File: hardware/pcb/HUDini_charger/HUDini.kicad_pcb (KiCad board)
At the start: 2 copper layers, 100 x 24 mm, 46 parts, among them J1 USB_C_Receptacle_PowerOnly_6P, J2 Conn_01x06_Pin, J3 Conn_01x06_Pin, J4 Conn_01x07_Pin, Q1 CHG (GDS), Q2 DSG (GDS), SW1 RESET, SW3 PWR_REC, U2 LM3671, U3 BQ29700DSER, U4 MCP73831-2-OT, U5 MDBT42Q-512K

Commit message: Updated PCB Files
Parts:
- removed C10: 100uF, Capacitor_SMD:C_0603_1608Metric
- removed C2: 10uF, Capacitor_SMD:C_0603_1608Metric
- removed C3: 0.1uF, Capacitor_SMD:C_0603_1608Metric
- removed D2, D3: D_Zener_Filled, Diode_SMD:D_SOD-323
- removed J1: USB_C_Receptacle_PowerOnly_6P, Connector_USB:USB_C_Receptacle_HRO_TYPE-C-31-M-12
- removed L1: 2.2uH, Inductor_SMD:L_1210_3225Metric
- removed U5: MDBT42Q-512K, RF_Module:Raytac_MDBT42Q
- added BT2: LIR2450, Connector_Wire:SolderWire-0.15sqmm_1x02_P4mm_D0.5mm_OD1.5mm, F.Cu at (167.5, 123.0)
- added C12: 10uF, Capacitor_SMD:C_0603_1608Metric_Pad1.08x0.95mm_HandSolder, F.Cu at (175.2, 72.0)
- added C13: 0.1uF, Capacitor_SMD:C_0603_1608Metric_Pad1.08x0.95mm_HandSolder, F.Cu at (175.2, 74.5)
- added C14: 10uF, Capacitor_SMD:C_0603_1608Metric_Pad1.08x0.95mm_HandSolder, F.Cu at (175.2, 77.0)
- added C15: 10uF, Capacitor_SMD:C_0603_1608Metric_Pad1.08x0.95mm_HandSolder, F.Cu at (175.2, 79.5)
- added J5: USB_C_Receptacle_USB2.0_14P, Connector_USB:USB_C_Receptacle_GCT_USB4085, F.Cu at (176.7, 122.6)
- added L2: 1.5uH, Inductor_SMD:L_0603_1608Metric_Pad1.05x0.95mm_HandSolder, F.Cu at (175.2, 82.1)
- added R18: 10K, Resistor_SMD:R_0603_1608Metric_Pad0.98x0.95mm_HandSolder, F.Cu at (246.6, 116.5)
- added R19: 10K, Resistor_SMD:R_0603_1608Metric_Pad0.98x0.95mm_HandSolder, F.Cu at (254.9, 122.5)
- added R20: 330, Resistor_SMD:R_0603_1608Metric_Pad0.98x0.95mm_HandSolder, F.Cu at (246.6, 122.5)
- added REF**: MountingHole_2.2mm_M2_DIN965_Pad, MountingHole:MountingHole_2.2mm_M2_DIN965_Pad, F.Cu at (167.5, 129.5)
- added REF**: MountingHole_2.2mm_M2_DIN965_Pad, MountingHole:MountingHole_2.2mm_M2_DIN965_Pad, F.Cu at (167.5, 112.5)
- added REF**: MountingHole_2.2mm_M2_DIN965_Pad, MountingHole:MountingHole_2.2mm_M2_DIN965_Pad, F.Cu at (262.5, 112.5)
- added REF**: MountingHole_2.2mm_M2_DIN965_Pad, MountingHole:MountingHole_2.2mm_M2_DIN965_Pad, F.Cu at (262.5, 129.5)
- added SW2: BOOT, Button_Switch_SMD:SW_SPST_PTS810, F.Cu at (241.5, 117.0)
- added SW5: SW_SPDT, Button_Switch_THT:SW_E-Switch_EG1224_SPDT_Angled, F.Cu at (189.5, 125.5)
- added U1: TPS63031DSK, Package_SON:WSON-10-1EP_2.5x2.5mm_P0.5mm_EP1.2x2mm, F.Cu at (180.2, 92.8)
- BT1: footprint Battery:BatteryHolder_Keystone_3009_1x2450 -> Connector_Wire:SolderWire-0.15sqmm_1x02_P4mm_D0.5mm_OD1.5mm
- C1: value 22uF -> 0.1uF; footprint Capacitor_SMD:C_0603_1608Metric -> Capacitor_SMD:C_0603_1608Metric_Pad1.08x0.95mm_HandSolder
- C11, C4, C5, C6, C8, C9: footprint Capacitor_SMD:C_0603_1608Metric -> Capacitor_SMD:C_0603_1608Metric_Pad1.08x0.95mm_HandSolder
- C7: value 1uF -> 10uF; footprint Capacitor_SMD:C_0603_1608Metric -> Capacitor_SMD:C_0603_1608Metric_Pad1.08x0.95mm_HandSolder
- D1, D4: footprint LED_SMD:LED_0603_1608Metric -> LED_SMD:LED_0603_1608Metric_Pad1.05x0.95mm_HandSolder
- J2: value Conn_01x06_Pin -> Conn_01x04_Pin; footprint Connector_PinHeader_2.54mm:PinHeader_1x06_P2.54mm_Vertical -> Connector_Wire:SolderWire-0.15sqmm_1x04_P4mm_D0.5mm_OD1.5mm
- J3: footprint Connector_PinHeader_2.54mm:PinHeader_1x06_P2.54mm_Vertical -> Connector_Wire:SolderWire-0.15sqmm_1x06_P4mm_D0.5mm_OD1.5mm
- J4: footprint Connector_PinHeader_2.54mm:PinHeader_1x07_P2.54mm_Horizontal -> Connector_PinHeader_1.00mm:PinHeader_1x07_P1.00mm_Horizontal
- R1, R12, R13, R14, R15, R16, R17, R2, R3, R4, R5, R6, R7, R8: footprint Resistor_SMD:R_0603_1608Metric -> Resistor_SMD:R_0603_1608Metric_Pad0.98x0.95mm_HandSolder
- R10: value 10K -> 22; footprint Resistor_SMD:R_0603_1608Metric -> Resistor_SMD:R_0603_1608Metric_Pad0.98x0.95mm_HandSolder
- R11: value 330 -> 22; footprint Resistor_SMD:R_0603_1608Metric -> Resistor_SMD:R_0603_1608Metric_Pad0.98x0.95mm_HandSolder
- R9: value 100K -> 10K; footprint Resistor_SMD:R_0603_1608Metric -> Resistor_SMD:R_0603_1608Metric_Pad0.98x0.95mm_HandSolder
- U2: value LM3671 -> ESP32-S3-MINI-1; footprint Package_TO_SOT_SMD:SOT-23-5 -> RF_Module:ESP32-S2-MINI-1
- moved SW3 151.3 mm to (254.0, 128.2)
- moved C9 146.8 mm to (258.9, 116.5)
- moved R13 142.8 mm to (258.9, 119.5)
- moved R12 138.6 mm to (254.8, 119.5)
- moved R14 138.5 mm to (259.0, 122.5)
- moved R17 134.8 mm to (254.8, 116.5)
- moved C11 134.6 mm to (246.6, 119.5)
- moved R15 130.3 mm to (250.7, 116.5)
- moved R16 130.3 mm to (250.7, 119.5)
- moved D4 126.2 mm to (250.8, 122.5)
- moved C8 123.8 mm to (235.9, 116.0)
- moved C7 123.4 mm to (235.9, 125.0)
- moved C6 123.4 mm to (235.9, 122.0)
- moved R9 119.4 mm to (235.9, 119.0)
- moved SW1 115.6 mm to (241.5, 122.5)
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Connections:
- BT1 pad 1: VBAT -> +BATT
- C1 pad 1: VBAT -> Net-(U3-BAT)
- C1 pad 2: GND -> B_GND
- C11 pad 1: GND -> Net-(U2-EN)
- C11 pad 2: Net-(U5-DEC4) -> GND
- C4 pad 1: VBAT -> +BATT
- J2 pad 3: /SWDCLK -> /UART_TX
- J2 pad 4: /SWDIO -> /UART_RX
- R10 pad 1: +3V3 -> USB_D-
- R10 pad 2: /BTN_PWRREC -> Net-(U2-USB_D-)
- R11 pad 1: /REC_LED -> USB_D+
- R11 pad 2: Net-(D4-A) -> Net-(U2-USB_D+)
- R13 pad 2: Net-(U5-TRACEDATA1/P0.16) -> Net-(U2-IO12)
- R14 pad 2: Net-(U5-TRACEDATA2/P0.15) -> Net-(U2-IO11)
- R15 pad 2: Net-(U5-P0.11) -> Net-(U2-IO4)
- R16 pad 2: Net-(U5-P0.12) -> Net-(U2-IO5)
- R17 pad 2: Net-(U5-P0.13) -> Net-(U2-IO6)
- R4 pad 1: VBAT -> +BATT
- R9 pad 1: /RESET -> Net-(U2-EN)
- SW1 pad 1: /RESET -> Net-(U2-EN)
- SW3 pad 1: /BTN_PWRREC -> /BTN_REC
- U2 pad 1: VBAT -> GND
- U2 pad 3: VBAT -> +3V3
- U2 pad 4: +3V3 -> Net-(U2-IO0)
- U2 pad 5: Net-(U2-SW) -> unconnected-(U2-IO1-Pad5)
- U4 pad 3: VBAT -> +BATT
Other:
- board size 100 x 24 mm -> 100 x 22 mm
- copper layers 2 -> 4

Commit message: new files
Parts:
- removed L2: 1.5uH, Inductor_SMD:L_0603_1608Metric_Pad1.05x0.95mm_HandSolder
- added L1: LPS3015-153MRC, footprints:IND_LPS3015_COC, F.Cu at (128.8, 92.1)
- C4, C5, C8: footprint Capacitor_SMD:C_0603_1608Metric_Pad1.08x0.95mm_HandSolder -> Capacitor_SMD:C_0603_1608Metric
- D1: footprint LED_SMD:LED_0603_1608Metric_Pad1.05x0.95mm_HandSolder -> LED_SMD:LED_0603_1608Metric
- Q1: value CHG (GDS) -> CSD17577Q3A; footprint Package_TO_SOT_SMD:SOT-23 -> footprints:DNH0008A
- Q2: value DSG (GDS) -> CSD17577Q3A; footprint Package_TO_SOT_SMD:SOT-23 -> footprints:DNH0008A
- R5, R6, R7, R8: footprint Resistor_SMD:R_0603_1608Metric_Pad0.98x0.95mm_HandSolder -> Resistor_SMD:R_0603_1608Metric
- moved R6 81.9 mm to (121.5, 87.5), turned to 180 degrees
- moved D1 80.8 mm to (118.2, 88.2), turned to 90 degrees
- moved C4 80.3 mm to (115.7, 93.2), turned to 90 degrees
- moved R5 79.2 mm to (121.5, 89.5)
- moved C5 77.8 mm to (122.7, 93.2), turned to 90 degrees
- moved U4 76.6 mm to (119.4, 92.5)
- moved U3 76.0 mm to (118.4, 78.0)
- moved C1 74.8 mm to (122.9, 81.5)
- moved R4 74.6 mm to (123.4, 78.0)
- moved R2 74.0 mm to (124.9, 74.0)
- moved R1 73.3 mm to (112.4, 79.5)
- moved R3 68.8 mm to (117.6, 82.5)
- moved SW5 66.6 mm to (127.7, 100.9)
- moved R7 66.2 mm to (115.8, 98.0)
- moved J2 66.1 mm to (141.7, 99.4)
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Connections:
- Q1 pad 1: Net-(Q1-G) -> Net-(Q1-Drain)
- Q1 pad 2: Net-(Q1-D) -> Net-(Q1-Gate)
- Q2 pad 1: Net-(Q2-G) -> Net-(Q1-Drain)
- Q2 pad 2: Net-(Q1-D) -> Net-(Q2-Gate)
- R1 pad 2: Net-(Q1-G) -> Net-(Q1-Gate)
- R2 pad 1: Net-(Q2-G) -> Net-(Q2-Gate)
- U3 pad 2: Net-(Q1-G) -> Net-(Q1-Gate)
- U3 pad 3: Net-(Q2-G) -> Net-(Q2-Gate)
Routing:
- added copper zone on In2.Cu, net +3V3
- added copper zone on In1.Cu, net GND

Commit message: More Progress
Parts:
- removed J2: Conn_01x04_Pin, Connector_Wire:SolderWire-0.15sqmm_1x04_P4mm_D0.5mm_OD1.5mm
- removed J5: USB_C_Receptacle_USB2.0_14P, Connector_USB:USB_C_Receptacle_GCT_USB4085
- removed U2: ESP32-S3-MINI-1, RF_Module:ESP32-S2-MINI-1
- added C2: 0.1uF, Capacitor_SMD:C_0603_1608Metric_Pad1.08x0.95mm_HandSolder, F.Cu at (84.0, 79.4)
- added C3: 4.7uF, Capacitor_SMD:C_0603_1608Metric_Pad1.08x0.95mm_HandSolder, F.Cu at (84.0, 81.9)
- added J1: USB_B_Micro, Connector_USB:USB_Micro-B_Amphenol_10103594-0001LF_Horizontal, F.Cu at (116.6, 105.4)
- added R9: 47.5K, Resistor_SMD:R_0603_1608Metric_Pad0.98x0.95mm_HandSolder, F.Cu at (84.0, 89.4)
- added U5: CP2102N-Axx-xQFN20, Package_DFN_QFN:SiliconLabs_QFN-20-1EP_3x3mm_P0.5mm_EP1.8x1.8mm, F.Cu at (93.5, 70.5)
- added U6: ESP32-WROOM-32E, RF_Module:ESP32-WROOM-32D, F.Cu at (163.8, 92.2)
- L1: footprint footprints:IND_LPS3015_COC -> footprints:LPS3015
- Q1, Q2: value CSD17577Q3A -> Q_NMOS_SSSGD_AvalancheRated; footprint footprints:DNH0008A -> Package_SON:VSON-8_3.3x3.3mm_P0.65mm_NexFET
- R7: value 5.1K -> 1K; footprint Resistor_SMD:R_0603_1608Metric -> Resistor_SMD:R_0603_1608Metric_Pad0.98x0.95mm_HandSolder
- R8: value 5.1K -> 22.1K; footprint Resistor_SMD:R_0603_1608Metric -> Resistor_SMD:R_0603_1608Metric_Pad0.98x0.95mm_HandSolder
- moved R8 37.5 mm to (84.0, 86.9)
- moved R7 34.6 mm to (84.0, 84.4)
- moved R10 21.7 mm to (142.8, 69.2)
- moved R11 21.7 mm to (142.8, 72.2)
- moved Q1 6.16 mm to (134.3, 70.8)
- moved Q2 6.16 mm to (134.3, 75.4)
- moved R6 5.54 mm to (116.3, 89.3)
- moved C5 5.52 mm to (117.4, 94.6)
- moved R5 5.48 mm to (116.3, 91.1)
- moved D1 5.44 mm to (113.2, 90.3)
- moved U4 5.22 mm to (114.4, 94.0)
- moved C4 4.69 mm to (111.1, 94.0)
- moved REF** 4.30 mm to (107.6, 83.6)
- moved REF** 4.21 mm to (202.9, 83.7)
- moved BT1 4.16 mm to (107.4, 92.8), turned to 90 degrees
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- renumbered C11 to C10, C12 to C11, C13 to C12, C14 to C13, C15 to C14, R9 to R10, R13 to R11, R14 to R12, R16 to R13, R15 to R14, R17 to R15, R12 to R16, R18 to R17, R19 to R18, R20 to R19
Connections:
- Q1 pad 1: Net-(Q1-Drain) -> GND
- Q1 pad 2: Net-(Q1-Gate) -> GND
- Q1 pad 4: (no net) -> Net-(Q1-G)
- Q1 pad 5: (no net) -> Net-(Q1-D)
- Q2 pad 1: Net-(Q1-Drain) -> B_GND
- Q2 pad 2: Net-(Q2-Gate) -> B_GND
- Q2 pad 4: (no net) -> Net-(Q2-G)
- Q2 pad 5: (no net) -> Net-(Q1-D)
- R1 pad 2: Net-(Q1-Gate) -> Net-(Q1-G)
- R2 pad 1: Net-(Q2-Gate) -> Net-(Q2-G)
- R7 pad 2: GND -> Net-(U5-VDD)
- R8 pad 2: GND -> 5V_USB
- U3 pad 2: Net-(Q1-Gate) -> Net-(Q1-G)
- U3 pad 3: Net-(Q2-Gate) -> Net-(Q2-G)
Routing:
- net 5V_USB: track 0.00 -> 16.9 mm, vias 0 -> 1
- net +BATT: track 0.00 -> 9.20 mm, vias 0 -> 1
- net +3V3: track 0.00 -> 7.89 mm, vias 0 -> 2
- net Net-(U1-EN): track 0.00 -> 5.36 mm
- net Net-(D1-A): track 0.00 -> 2.37 mm
- net Net-(D1-K): track 0.00 -> 2.10 mm
- net Net-(U4-PROG): track 0.00 -> 1.90 mm
- added copper zone on F.Cu, net +3V3
- added copper zone on F.Cu, net +BATT
- added copper zone on F.Cu, net 5V_USB
- added copper zone on F.Cu, net GND
- added copper zone on F.Cu, net Net-(SW5-C)
- added copper zone on F.Cu, net Net-(U1-L1)
- added copper zone on F.Cu, net Net-(U1-L2)
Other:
- board size 100 x 22 mm -> 100 x 27 mm

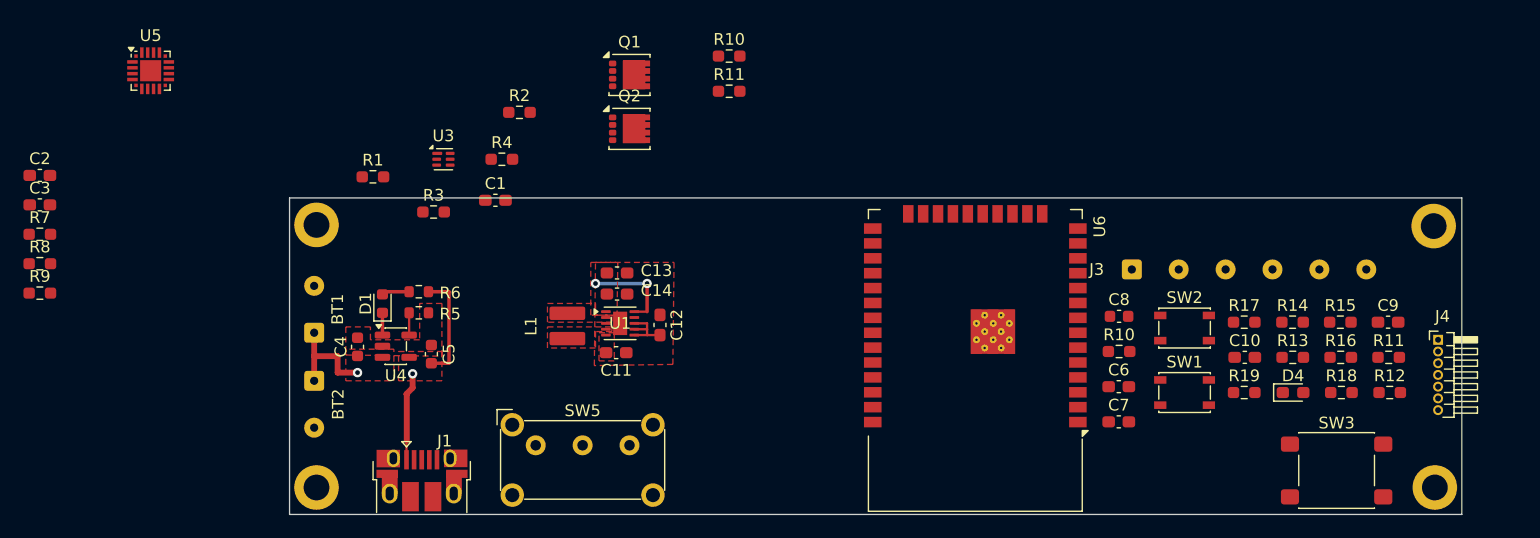
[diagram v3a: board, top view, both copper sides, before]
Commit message: Some Components Finished Wiring
Buck-Boost Converter, USB-to-UART, Protection, Charger. Next step is every connection to ESP32
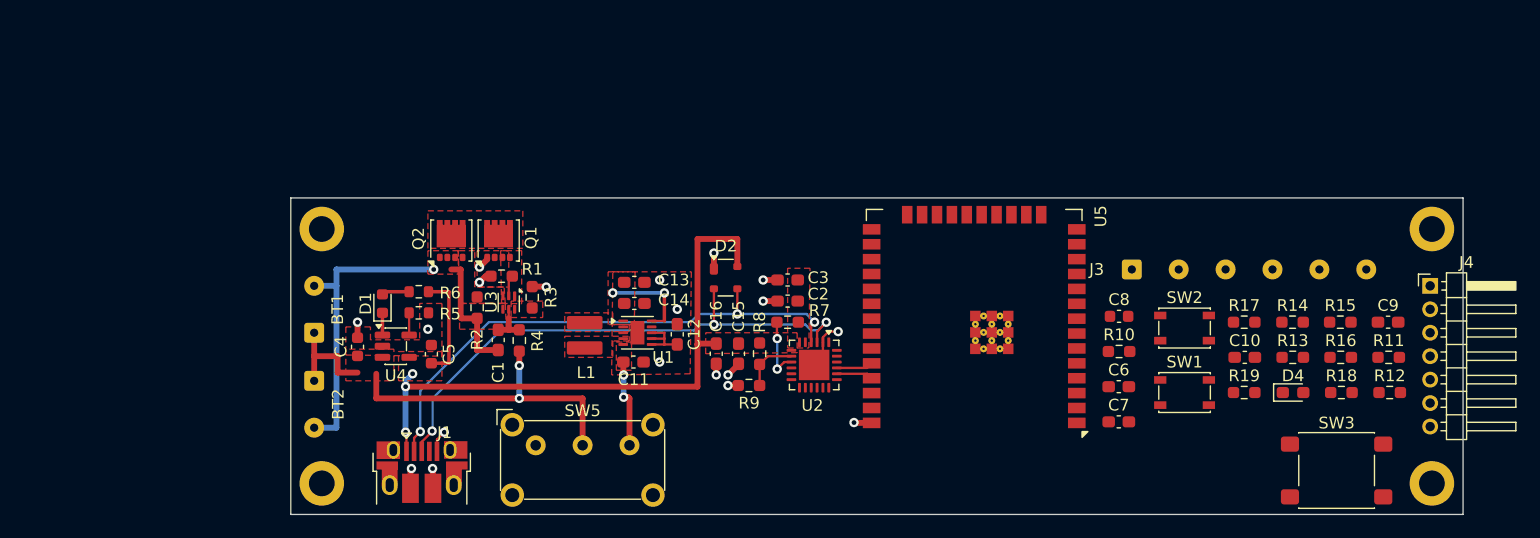
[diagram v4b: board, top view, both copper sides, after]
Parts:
- removed the R10 at (142.8, 69.2)
- removed the R11 at (142.8, 72.2)
- removed the U5 at (93.5, 70.5)
- added C15: 4.7uF, Capacitor_SMD:C_0603_1608Metric_Pad1.08x0.95mm_HandSolder, F.Cu at (143.6, 94.6)
- added C16: 0.1uF, Capacitor_SMD:C_0603_1608Metric_Pad1.08x0.95mm_HandSolder, F.Cu at (141.7, 94.6)
- added D2: SP0503BAHT, Package_TO_SOT_SMD:SOT-143, F.Cu at (142.5, 88.1)
- added U2: CP2102N-Axx-xQFN24, Package_DFN_QFN:QFN-24-1EP_4x4mm_P0.5mm_EP2.6x2.6mm, F.Cu at (150.1, 95.5)
- J4: footprint Connector_PinHeader_1.00mm:PinHeader_1x07_P1.00mm_Horizontal -> Connector_PinHeader_2.00mm:PinHeader_1x07_P2.00mm_Horizontal
- U5: renamed from U6; footprint RF_Module:ESP32-WROOM-32D -> RF_Module:ESP32-WROOM-32E
- moved C2 64.7 mm to (147.8, 90.1), turned to 180 degrees
- moved R7 64.2 mm to (147.8, 91.9)
- moved C3 64.1 mm to (147.8, 88.3), turned to 180 degrees
- moved R8 61.9 mm to (145.4, 94.6), turned to 90 degrees
- moved R9 61.0 mm to (144.5, 97.3)
- moved Q1 18.0 mm to (123.1, 84.9), turned to 90 degrees
- moved Q2 18.0 mm to (119.1, 84.9), turned to 90 degrees
- moved R2 17.0 mm to (121.3, 90.7), turned to -90 degrees
- moved R4 15.5 mm to (124.9, 93.5), turned to 90 degrees
- moved R1 13.9 mm to (123.4, 88.0)
- moved U3 13.4 mm to (124.0, 90.2), turned to -90 degrees
- moved C1 11.9 mm to (123.1, 93.4), turned to -90 degrees
- moved R3 11.1 mm to (126.0, 89.8), turned to 90 degrees
- moved J4 4.65 mm to (202.6, 88.8)
- moved U5 3.06 mm to (163.7, 95.2)
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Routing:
- net USB_D+: track 0.00 -> 46.7 mm, vias 0 -> 3
- net USB_D-: track 0.00 -> 46.0 mm, vias 0 -> 3
- net 5V_USB: track 16.9 -> 61.2 mm, vias 1 -> 3
- net B_GND: track 0.00 -> 36.5 mm, vias 0 -> 1
- net +BATT: track 9.20 -> 36.9 mm, vias 1 -> 2
- net GND: track 0.00 -> 22.8 mm, vias 0 -> 19
- net Net-(SW5-C): track 0.00 -> 7.60 mm, vias 0 -> 2
- net Net-(U2-~{RST}): track 0.00 -> 5.47 mm, vias 0 -> 2
- net Net-(U2-VBUS): track 0.00 -> 4.80 mm
- net Net-(U3-BAT): track 0.00 -> 3.55 mm
- net /ESP_RX: track 0.00 -> 3.13 mm
- net /ESP_TX: track 0.00 -> 3.12 mm
- net Net-(Q1-G): track 0.00 -> 1.80 mm
- added copper zone on F.Cu, net B_GND
- added copper zone on F.Cu, net Net-(Q1-D)
- added copper zone on F.Cu, net Net-(Q1-G)
- added copper zone on F.Cu, net Net-(Q2-G)
- added copper zone on F.Cu, net Net-(U2-VDD)
- added copper zone on F.Cu, net Net-(U3-V-)

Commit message: Updated PCB
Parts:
- C4, C5, C8: footprint Capacitor_SMD:C_0603_1608Metric -> Capacitor_SMD:C_0603_1608Metric_Pad1.08x0.95mm_HandSolder
- D1: footprint LED_SMD:LED_0603_1608Metric -> LED_SMD:LED_0603_1608Metric_Pad1.05x0.95mm_HandSolder
- R5, R6: footprint Resistor_SMD:R_0603_1608Metric -> Resistor_SMD:R_0603_1608Metric_Pad0.98x0.95mm_HandSolder
- moved C10 10.9 mm to (175.9, 94.1)
- moved R18 10.3 mm to (184.7, 98.1)
- moved RESET 9.65 mm to (176.1, 90.0), turned to 90 degrees
- moved C8 7.78 mm to (175.5, 83.6), turned to -90 degrees
- moved R19 6.66 mm to (193.4, 98.2)
- moved R16 6.57 mm to (189.3, 98.2)
- moved D4 6.53 mm to (197.4, 98.2), turned to 180 degrees
- moved R13 6.18 mm to (190.0, 88.8), turned to -90 degrees
- moved R12 5.55 mm to (194.4, 95.0), turned to 180 degrees
- moved R11 5.48 mm to (194.4, 92.0), turned to 180 degrees
- moved R14 4.96 mm to (187.0, 88.8), turned to -90 degrees
- moved J3 4.16 mm to (178.3, 83.4)
- moved R17 4.13 mm to (184.0, 88.8), turned to -90 degrees
- moved R15 3.23 mm to (194.5, 88.7), turned to 180 degrees
- moved C9 3.16 mm to (198.4, 88.8), turned to 180 degrees
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- renumbered SW2 to BOOT, SW1 to RESET
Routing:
- net /HUD_RST: track 0.00 -> 58.8 mm, vias 0 -> 4
- net /HUD_CS: track 0.00 -> 54.1 mm, vias 0 -> 2
- net /BTN_REC: track 0.00 -> 52.1 mm, vias 0 -> 2
- net Net-(U5-IO18): track 0.00 -> 51.0 mm
- net /HUD_DC: track 0.00 -> 50.3 mm, vias 0 -> 4
- net Net-(U5-IO23): track 0.00 -> 49.9 mm, vias 0 -> 4
- net Net-(U5-IO34): track 0.00 -> 40.6 mm, vias 0 -> 2
- net Net-(U5-IO0): track 0.00 -> 36.1 mm, vias 0 -> 2
- net Net-(U5-IO25): track 0.00 -> 30.9 mm, vias 0 -> 2
- net /REC_LED: track 0.00 -> 28.7 mm, vias 0 -> 2
- net Net-(U5-IO26): track 0.00 -> 26.4 mm, vias 0 -> 2
- net +3V3: track 7.89 -> 29.7 mm, vias 2 -> 11
- net GND: track 22.8 -> 43.3 mm, vias 19 -> 33
- net Net-(U5-EN): track 0.00 -> 16.3 mm, vias 0 -> 2
- net /HUD_CLK: track 0.00 -> 7.58 mm
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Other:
- board text added: "HUDini"

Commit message: Retry
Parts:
- renumbered RESET to SW1, BOOT to SW2
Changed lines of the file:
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@@
 			)
 		)
-		(property "Datasheet" ""
+		(property "Datasheet" "~"
 			(at 0 0 90)
 			(layer "F.Fab")
@@
 			)
 		)
-		(property "Description" ""
+		(property "Description" "Unpolarized capacitor"
 			(at 0 0 90)
 			(layer "F.Fab")
@@
 			)
 		)
-		(property "Datasheet" ""
+		(property "Datasheet" "~"
 			(at 0 0 90)
 			(layer "F.Fab")
@@
 			)
 		)
-		(property "Description" ""
+		(property "Description" "Unpolarized capacitor"
 			(at 0 0 90)
 			(layer "F.Fab")
@@
 			)
 		)
-		(property "Datasheet" ""
+		(property "Datasheet" "~"
 			(at 0 0 90)
 			(layer "F.Fab")
@@
 			)
 		)
-		(property "Description" ""
+		(property "Description" "Light emitting diode"
 			(at 0 0 90)
 			(layer "F.Fab")
@@
 		(descr "C&K Components, PTS 810 Series, Microminiature SMT Top Actuated, http://www.ckswitches.com/media/1476/pts810.pdf")
 		(tags "SPST Button Switch")
-		(property "Reference" "RESET"
+		(property "Reference" "SW1"
 			(at 3.6 0 180)
 			(layer "F.SilkS")
@@
 			)
 		)
-		(property "Datasheet" ""
+		(property "Datasheet" "~"
 			(at 0 0 90)
 			(layer "F.Fab")
@@
 			)
 		)
-		(property "Description" ""
+		(property "Description" "Unpolarized capacitor"
 			(at 0 0 90)
 			(layer "F.Fab")
@@
 			)
 		)
-		(property "Datasheet" ""
+		(property "Datasheet" "~"
 			(at 0 0 180)
 			(layer "F.Fab")
@@
 			)
 		)
-		(property "Description" ""
+		(property "Description" "Resistor"
 			(at 0 0 180)
 			(layer "F.Fab")
@@
 			)
 		)
-		(property "Datasheet" ""
+		(property "Datasheet" "~"
 			(at 0 0 0)
 			(layer "F.Fab")
@@
 			)
 		)
-		(property "Description" ""
+		(property "Description" "Resistor"
 			(at 0 0 0)
 			(layer "F.Fab")
@@
 		(descr "C&K Components, PTS 810 Series, Microminiature SMT Top Actuated, http://www.ckswitches.com/media/1476/pts810.pdf")
 		(tags "SPST Button Switch")
-		(property "Reference" "BOOT"
+		(property "Reference" "SW2"
 			(at -3.6 -0.1 180)
 			(layer "F.SilkS")
